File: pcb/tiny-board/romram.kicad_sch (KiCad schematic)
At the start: 6 parts, among them U4 74AC10, U5 SST39SF040, U6 62256-55

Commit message: Revising TINY board and creating test ROM for TINY board
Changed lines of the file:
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@@
 (kicad_sch
-	(version 20231120)
+	(version 20250114)
 	(generator "eeschema")
-	(generator_version "8.0")
+	(generator_version "9.0")
 	(paper "A4")
 	(title_block
@@
 		(date "2025-01-25")
 		(rev "1")
+	)
+	(text "LOW MEMORY"
+		(exclude_from_sim no)
+		(at 106.68 39.116 0)
+		(effects
+			(font
+				(size 1.27 1.27)
+			)
+		)
+	)
+	(text "ROM"
+		(exclude_from_sim no)
+		(at 48.514 31.496 0)
+		(effects
+			(font
+				(size 1.27 1.27)
+			)
+		)
+	)
+	(text "RAM / ROM"
+		(exclude_from_sim no)
+		(at 24.892 16.256 0)
+		(effects
+			(font
+				(size 2.54 2.54)
+				(thickness 0.508)
+				(bold yes)
+			)
+		)
+	)
+	(text "0x0000-0x7EFF\n(32 KiB)\n[~{A15} & I/O]"
+		(exclude_from_sim no)
+		(at 106.68 44.704 0)
+		(effects
+			(font
+				(size 1.27 1.27)
+			)
+		)
+	)
+	(text "0xC000-0xFFFF\n(16 KiB)"
+		(exclude_from_sim no)
+		(at 48.768 37.084 0)
+		(effects
+			(font
+				(size 1.27 1.27)
+			)
+		)
 	)
 	(junction
@@
 		)
 	)
-	(text "LOW MEMORY"
-		(exclude_from_sim no)
-		(at 106.68 39.116 0)
-		(effects
-			(font
-				(size 1.27 1.27)
-			)
-		)
-	)
-	(text "ROM"
-		(exclude_from_sim no)
-		(at 48.514 31.496 0)
-		(effects
-			(font
-				(size 1.27 1.27)
-			)
-		)
-	)
-	(text "RAM / ROM"
-		(exclude_from_sim no)
-		(at 24.892 16.256 0)
-		(effects
-			(font
-				(size 2.54 2.54)
-				(thickness 0.508)
-				(bold yes)
-			)
-		)
-	)
-	(text "0x0000-0x7EFF\n(32 KiB)\n[~{A15} & I/O]"
-		(exclude_from_sim no)
-		(at 106.68 44.704 0)
-		(effects
-			(font
-				(size 1.27 1.27)
-			)
-		)
-	)
-	(text "0xC000-0xFFFF\n(16 KiB)"
-		(exclude_from_sim no)
-		(at 48.768 37.084 0)
-		(effects
-			(font
-				(size 1.27 1.27)
-			)
-		)
-	)

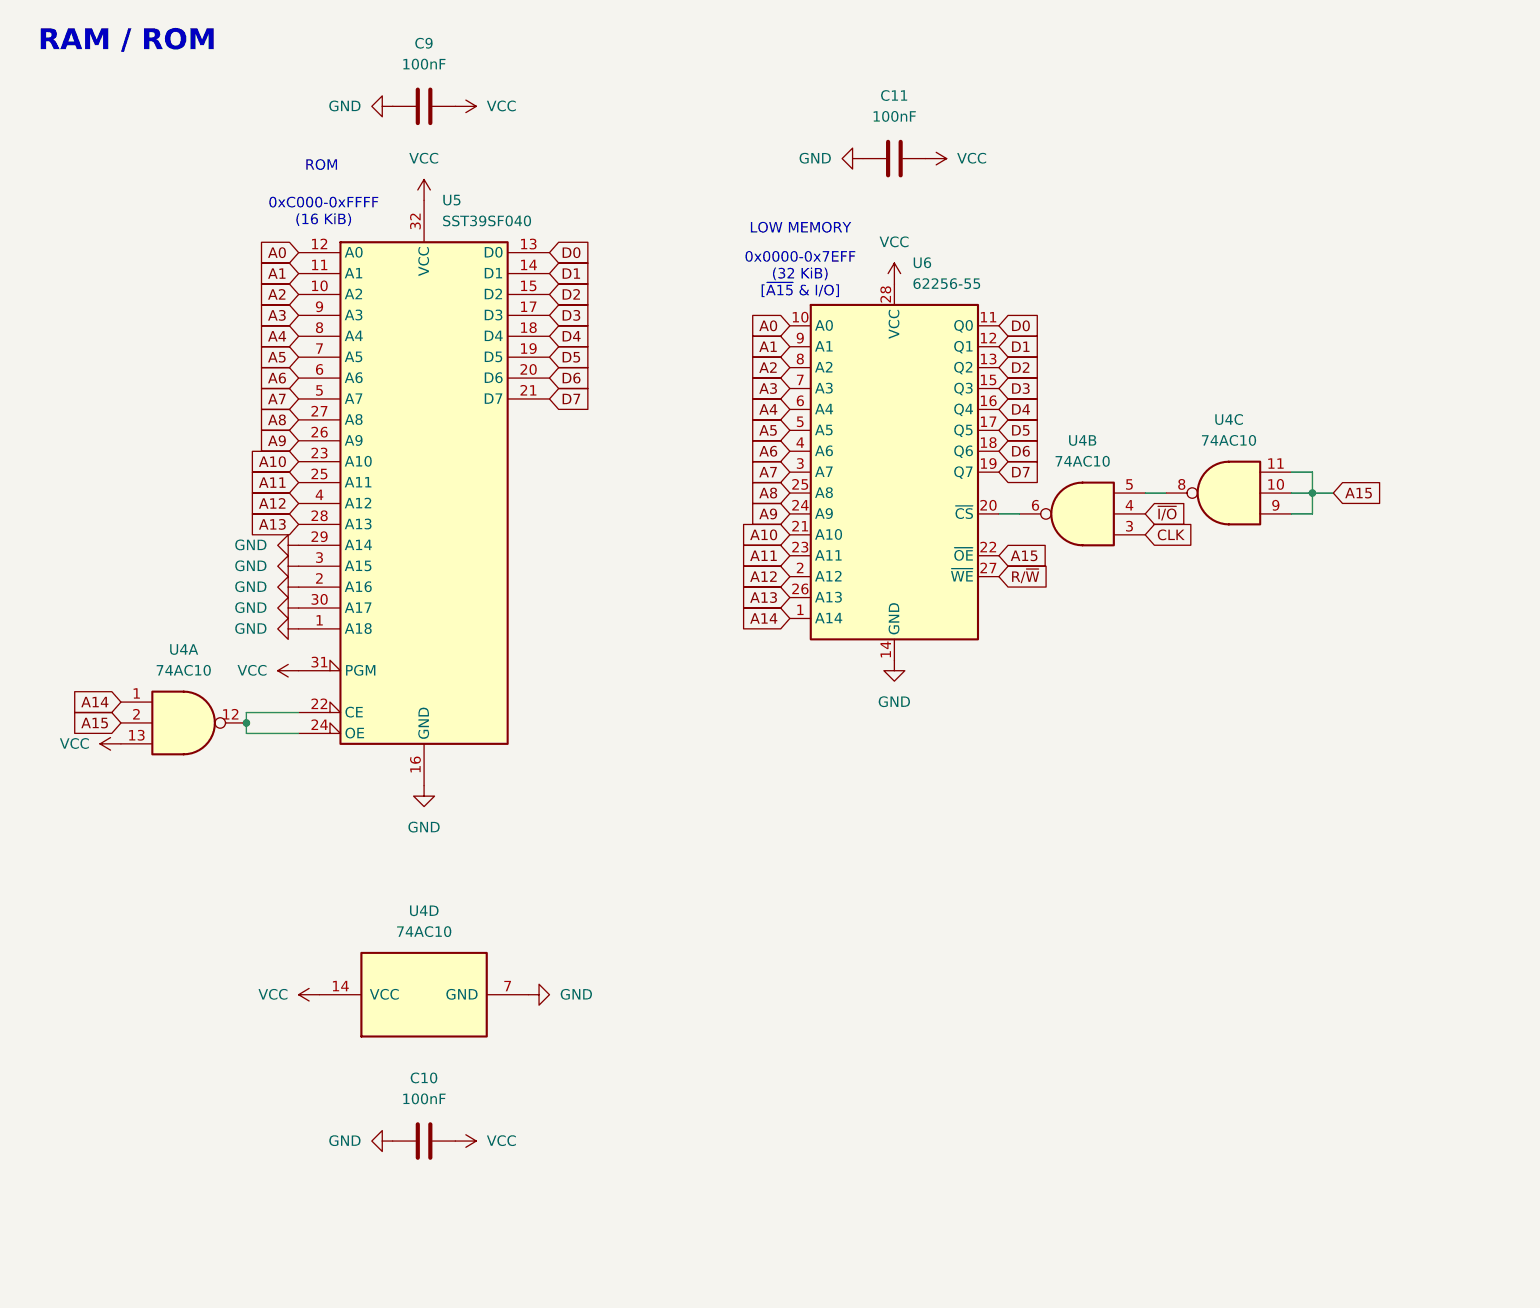
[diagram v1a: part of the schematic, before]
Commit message: Revising TINY board and writing CUPL
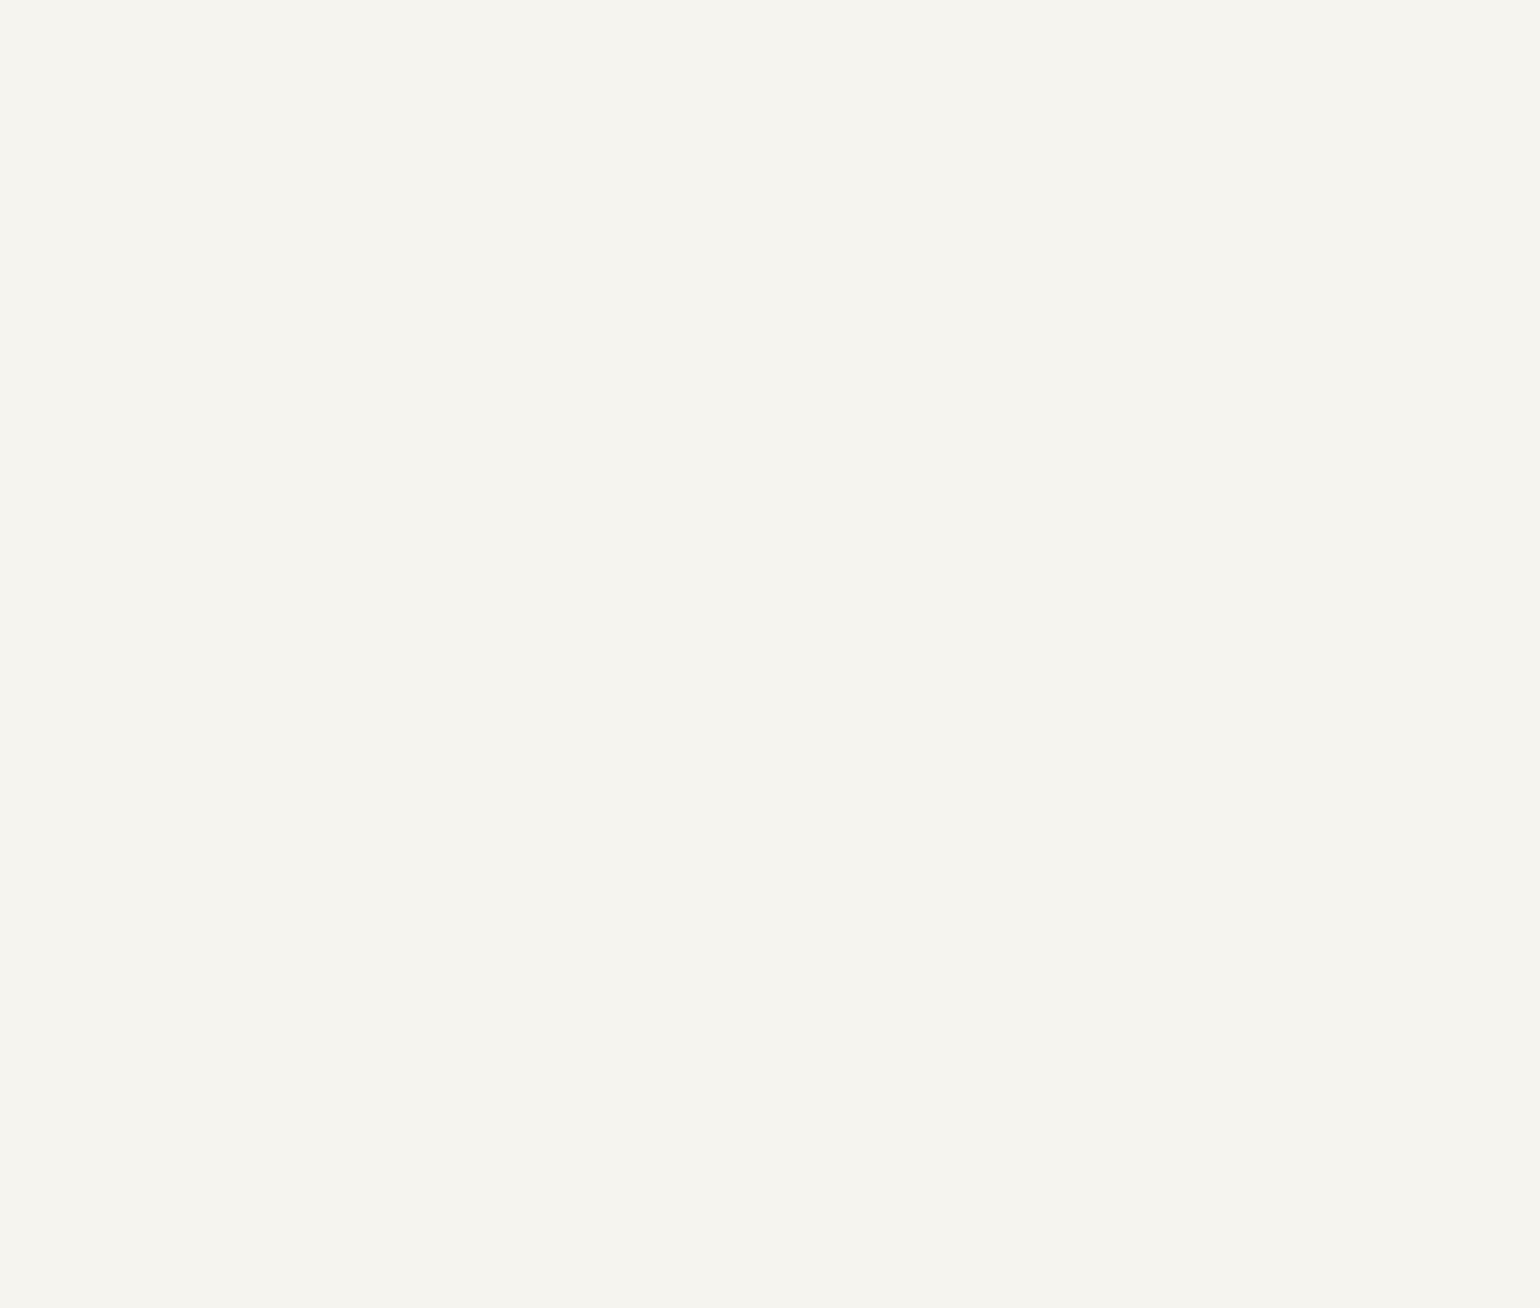
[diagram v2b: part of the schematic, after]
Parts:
- removed C10, C11, C9: 100nF, Capacitor_THT:C_Disc_D5.0mm_W2.5mm_P5.00mm, symbol Device:C
- removed U4: 74AC10, Package_DIP:DIP-14_W7.62mm_Socket, symbol 74xx:74LS10
- removed U5: SST39SF040, Package_DIP:DIP-32_W15.24mm_Socket, symbol Memory_Flash:SST39SF040
- removed U6: 62256-55, Package_DIP:DIP-28_W15.24mm_Socket, symbol Memory_RAM:CY62256-70PC
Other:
- note removed: "0x0000-0x7EFF (32 KiB) [~{A15} & I/O]"
- note removed: "0xC000-0xFFFF (16 KiB)"
- note removed: "LOW MEMORY"
- note removed: "RAM / ROM"
- note removed: "ROM"
